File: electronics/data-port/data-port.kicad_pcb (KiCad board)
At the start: 2 copper layers, 40 x 17 mm, 11 parts, among them J1 DATA, J2 LEAD, U1 USBLC6-2SC6

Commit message: DATA port: 100 nF at the ESD's VBUS pin (DP-5)
The kicad-happy review's DP-5: ST's USBLC6 datasheet (section 2.3,
Fig. 18) puts 100 nF right at VBUS (pin 5).  Here the nearest was C1,
4.9 mm away in a straight line but about 28 mm of track, and the
datasheet audit wrongly gave 4.5 mm.  C3, a 100 nF 0402 (C1525, basic,
already on the DATA x4 v2), now sits on the thin track that feeds
U1.5.  It is 0.7 mm pad to pad from the pin, between J2's and U1's
courtyards (1.36 mm apart: an 0603 doesn't fit), with its own GND via
at (18.3, 10.72).  The feed track now ends at C3.1's centre, so
Freerouting sees the pad joined.

J2's open pins 1-3 lose their "·" labels: C3 sits under pin 3.  The
datasheet audit's line and docs/electronics.md say so.

No routing change: every track and via is the previous commit's.  The
JLC snapshot gains the board's C1525 line; the order's total stays the
quote's.  ERC 0, DRC 0, unconnected 0, parity 0.

Co-Authored-By: Claude Opus 5.5 <noreply@anthropic.com>
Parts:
- added C3: 100n, Capacitor_SMD:C_0402_1005Metric, F.Cu at (16.9, 10.7)
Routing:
- net GND: track 6.18 -> 7.12 mm, vias 26 -> 27
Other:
- board text removed: "·"

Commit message: DATA port: a second GND test pad by the receptacle (DP-6)
The kicad-happy review's DP-6: Eve's rule wants GND spread, and the
port had one GND pad (TP1, by the lead).  TP3 is a bare 1.5 mm pad on
B.Cu at (32.95, 5.95), by the receptacle, named GND on B.SilkS and kept
out of the BOM and the CPL.  It sits on the stitching via that was
already there, now drawn so it stays.  It is 2.85 mm from H2's hole.

No routing change.  ERC 0, DRC 0, unconnected 0, parity 0.

Co-Authored-By: Claude Opus 5.5 <noreply@anthropic.com>
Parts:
- added TP3: GND, TestPoint:TestPoint_Pad_D1.5mm, B.Cu at (33.0, 5.95)

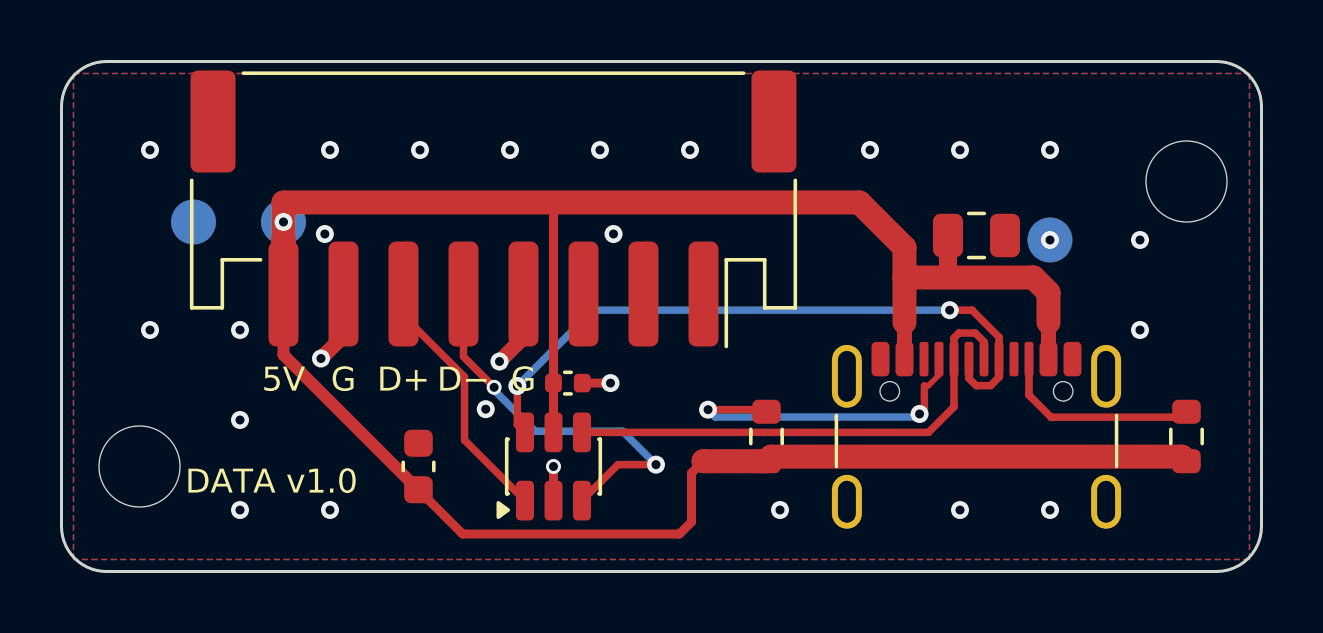
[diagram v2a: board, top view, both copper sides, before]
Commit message: DATA port: its antennas off, a dangling track now a DRC error
tools/kicad.sh data-port --clean (pcbgen.clean_antennas), on the
routed board as it was, no re-route.  Four router leftovers go:
- a doubled VBUS run on F.Cu from TP2 (the VBUS test pad) towards J2
  (the lead's PH 8): the shorter track lay along the other;
- a 7 µm VBUS dot on F.Cu near R1 (CC1's 56k Rp);
- a 97 µm CC1 step at R1's pad 2, folded into its neighbours;
- a 95 µm LEAD_DN stub on B.Cu inside its own via.
ERC, DRC (0), the flow-through check and connectivity are unchanged.
data-port leaves electronics/antennas.json's pending list:
test_antennas now holds it to none.  Its .kicad_pro makes a dangling
track or via an error, as write_via_rules now writes it.

Co-Authored-By: Claude Opus 5.5 <noreply@anthropic.com>
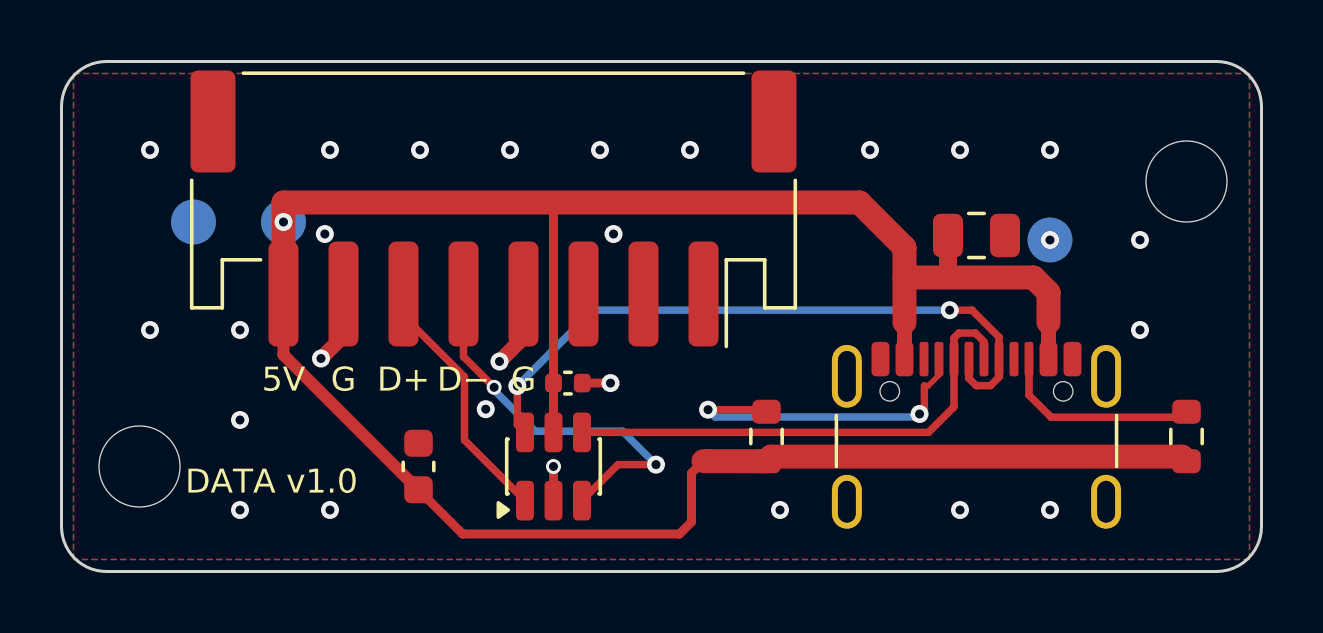
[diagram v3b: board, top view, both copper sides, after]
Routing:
- net /Port/VBUS: track 98.3 -> 97.2 mm
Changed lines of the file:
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@@
 	(segment
 		(start 23.5 13.325)
-		(end 21.405 13.325)
+		(end 21.4 13.32)
 		(width 0.8)
 		(layer "F.Cu")
@@
 	)
 	(segment
-		(start 21.405 13.325)
-		(end 21.4 13.32)
-		(width 0.8)
-		(layer "F.Cu")
-		(net "/Port/VBUS")
-	)
-	(segment
 		(start 7.4 9)
 		(end 7.4 7.75)
@@
 	)
 	(segment
-		(start 7.4 5.9)
-		(end 7.4 7)
-		(width 0.8)
-		(layer "F.Cu")
-		(net "/Port/VBUS")
-	)
-	(segment
 		(start 7.4 7)
 		(end 7.4 7.75)
@@
 	)
 	(segment
-		(start 23.4312 11.6062)
-		(end 23.5 11.675)
-		(width 0.25)
-		(layer "F.Cu")
-		(net "/Port/CC1")
-	)
-	(segment
 		(start 29.25 10.2757)
 		(end 29.25 10.4513)
@@
 		(width 0.25)
 		(layer "B.Cu")
-		(net "/Port/LEAD_DN")
-	)
-	(segment
-		(start 14.4212 10.9558)
-		(end 14.4212 10.8609)
-		(width 0.25)
-		(layer "B.Cu")
